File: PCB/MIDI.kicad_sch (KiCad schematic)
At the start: 17 parts, among them J6 MIDI Out, J7 MIDI In, U5 74LVC4245A, U6 6N137

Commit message: fixed PCB
 * Added 5.1k resistors to CC lines on USB-C port
 * Replaced diode OR thing and MOSFET with too low of a threshold voltage with a real OR gate and buffer
 * Fixed polarity of BNC output
 * Made headphone output not murderously loud and asymmetric
 * Added direct in/out to expansion pins
 * Reduced impedance into ADC for average volume level sensing
 * Increased MIDI input pullup resistance
 * Made thermal spokes to copper planes thinner
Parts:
- removed R22: 47, Resistor_SMD:R_0603_1608Metric_Pad0.98x0.95mm_HandSolder, symbol Device:R_US
- R21: value 47 -> 220
- renumbered D14 to D8
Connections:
- net MIDI In: now also R21.2
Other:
- moved on the sheet: R21
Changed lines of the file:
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@@
+    (stroke (width 0) (type default) (color 0 0 0 0))
+  )
+  (wire (pts (xy 99.695 76.2) (xy 99.695 80.01))
     (stroke (width 0) (type default) (color 0 0 0 0))
   )
@@
     (stroke (width 0) (type default) (color 0 0 0 0))
   )
+  (wire (pts (xy 99.695 80.01) (xy 118.745 80.01))
+    (stroke (width 0) (type default) (color 0 0 0 0))
+  )
+  (wire (pts (xy 99.695 64.77) (xy 99.695 68.58))
+    (stroke (width 0) (type default) (color 0 0 0 0))
+  )
   (wire (pts (xy 161.29 74.295) (xy 161.29 80.01))
     (stroke (width 0) (type default) (color 0 0 0 0))
@@
     (stroke (width 0) (type default) (color 0 0 0 0))
   )
+  (wire (pts (xy 118.745 64.77) (xy 118.745 74.93))
+    (stroke (width 0) (type default) (color 0 0 0 0))
+  )
+  (wire (pts (xy 149.86 113.665) (xy 145.415 113.665))
+    (stroke (width 0) (type default) (color 0 0 0 0))
+  )
+  (wire (pts (xy 149.86 114.935) (xy 149.86 113.665))
+    (stroke (width 0) (type default) (color 0 0 0 0))
+  )
+  (wire (pts (xy 167.64 121.92) (xy 167.64 123.825))
+    (stroke (width 0) (type default) (color 0 0 0 0))
+  )
+  (wire (pts (xy 108.585 129.54) (xy 110.49 129.54))
+    (stroke (width 0) (type default) (color 0 0 0 0))
+  )
+  (wire (pts (xy 153.67 77.47) (xy 168.91 77.47))
+    (stroke (width 0) (type default) (color 0 0 0 0))
+  )
+  (wire (pts (xy 125.095 118.11) (xy 125.095 123.825))
+    (stroke (width 0) (type default) (color 0 0 0 0))
+  )
+  (wire (pts (xy 108.585 118.11) (xy 108.585 123.825))
+    (stroke (width 0) (type default) (color 0 0 0 0))
+  )
+  (wire (pts (xy 133.985 85.09) (xy 138.43 85.09))
+    (stroke (width 0) (type default) (color 0 0 0 0))
+  )
   (wire (pts (xy 96.52 80.01) (xy 99.695 80.01))
-    (stroke (width 0) (type default) (color 0 0 0 0))
-  )
-  (wire (pts (xy 118.745 64.77) (xy 118.745 74.93))
-    (stroke (width 0) (type default) (color 0 0 0 0))
-  )
-  (wire (pts (xy 149.86 113.665) (xy 145.415 113.665))
-    (stroke (width 0) (type default) (color 0 0 0 0))
-  )
-  (wire (pts (xy 149.86 114.935) (xy 149.86 113.665))
-    (stroke (width 0) (type default) (color 0 0 0 0))
-  )
-  (wire (pts (xy 167.64 121.92) (xy 167.64 123.825))
-    (stroke (width 0) (type default) (color 0 0 0 0))
-  )
-  (wire (pts (xy 108.585 129.54) (xy 110.49 129.54))
-    (stroke (width 0) (type default) (color 0 0 0 0))
-  )
-  (wire (pts (xy 153.67 77.47) (xy 168.91 77.47))
-    (stroke (width 0) (type default) (color 0 0 0 0))
-  )
-  (wire (pts (xy 125.095 118.11) (xy 125.095 123.825))
-    (stroke (width 0) (type default) (color 0 0 0 0))
-  )
-  (wire (pts (xy 108.585 118.11) (xy 108.585 123.825))
-    (stroke (width 0) (type default) (color 0 0 0 0))
-  )
-  (wire (pts (xy 133.985 85.09) (xy 138.43 85.09))
-    (stroke (width 0) (type default) (color 0 0 0 0))
-  )
-  (wire (pts (xy 99.695 80.01) (xy 118.745 80.01))
     (stroke (width 0) (type default) (color 0 0 0 0))
   )
@@
   (symbol (lib_id "Device:D") (at 138.43 81.28 270) (unit 1)
     (in_bom yes) (on_board yes) (fields_autoplaced)
-    (property "Reference" "D14" (id 0) (at 140.462 81.7138 90)
+    (property "Reference" "D8" (id 0) (at 140.462 81.7138 90)
       (effects (font (size 1.27 1.27)) (justify left))
     )
@@
     (pin "2")
   )
-  (symbol (lib_id "Device:R_US") (at 99.695 76.2 0) (unit 1)
-    (in_bom yes) (on_board yes) (fields_autoplaced)
-    (property "Reference" "R22" (id 0) (at 101.346 75.3653 0)
-      (effects (font (size 1.27 1.27)) (justify left))
-    )
-    (property "Value" "47" (id 1) (at 101.346 77.9022 0)
-      (effects (font (size 1.27 1.27)) (justify left))
-    )
-    (property "Footprint" "Resistor_SMD:R_0603_1608Metric_Pad0.98x0.95mm_HandSolder" (id 2) (at 100.711 76.454 90)
-      (effects (font (size 1.27 1.27)) hide)
-    )
-    (property "Datasheet" "~" (id 3) (at 99.695 76.2 0)
-      (effects (font (size 1.27 1.27)) hide)
-    )
-    (pin "1")
-    (pin "2")
-  )
   (symbol (lib_id "Device:FerriteBead_Small") (at 151.13 77.47 270) (unit 1)
     (in_bom yes) (on_board yes) (fields_autoplaced)
@@
     (pin "2")
   )
-  (symbol (lib_id "Device:R_US") (at 99.695 68.58 0) (unit 1)
-    (in_bom yes) (on_board yes) (fields_autoplaced)
-    (property "Reference" "R21" (id 0) (at 101.346 67.7453 0)
+  (symbol (lib_id "Device:R_US") (at 99.695 72.39 0) (unit 1)
+    (in_bom yes) (on_board yes) (fields_autoplaced)
+    (property "Reference" "R21" (id 0) (at 101.346 71.5553 0)
       (effects (font (size 1.27 1.27)) (justify left))
     )
-    (property "Value" "47" (id 1) (at 101.346 70.2822 0)
+    (property "Value" "220" (id 1) (at 101.346 74.0922 0)
       (effects (font (size 1.27 1.27)) (justify left))
     )
-    (property "Footprint" "Resistor_SMD:R_0603_1608Metric_Pad0.98x0.95mm_HandSolder" (id 2) (at 100.711 68.834 90)
-      (effects (font (size 1.27 1.27)) hide)
-    )
-    (property "Datasheet" "~" (id 3) (at 99.695 68.58 0)
-      (effects (font (size 1.27 1.27)) hide)
-    )
+    (property "Footprint" "Resistor_SMD:R_0603_1608Metric_Pad0.98x0.95mm_HandSolder" (id 2) (at 100.711 72.644 90)
+      (effects (font (size 1.27 1.27)) hide)
+    )
+    (property "Datasheet" "~" (id 3) (at 99.695 72.39 0)
+      (effects (font (size 1.27 1.27)) hide)
+    )

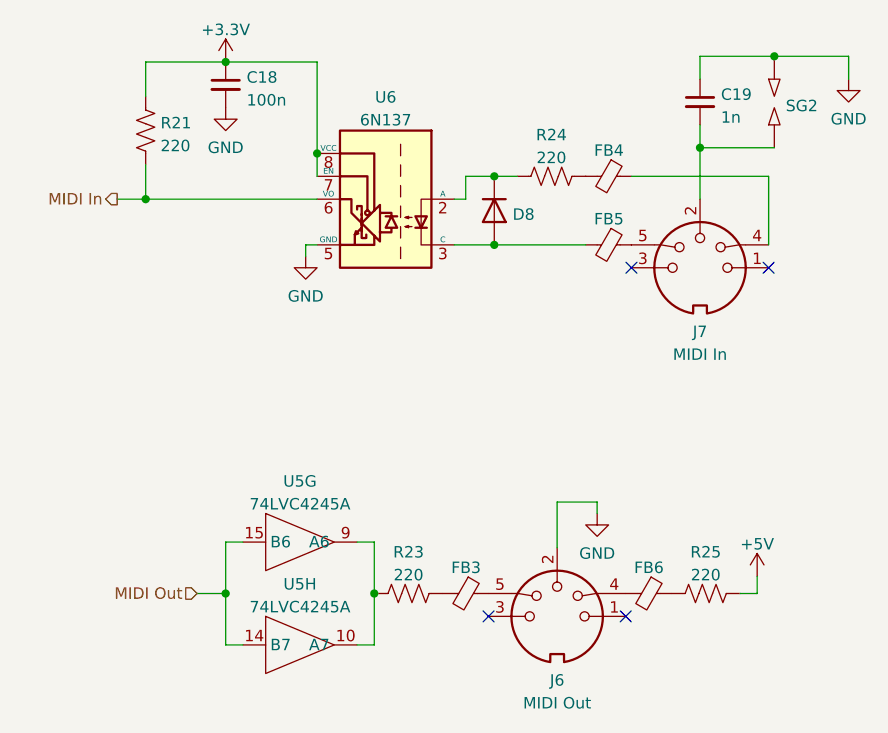
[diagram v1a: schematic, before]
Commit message: improved power line filtering
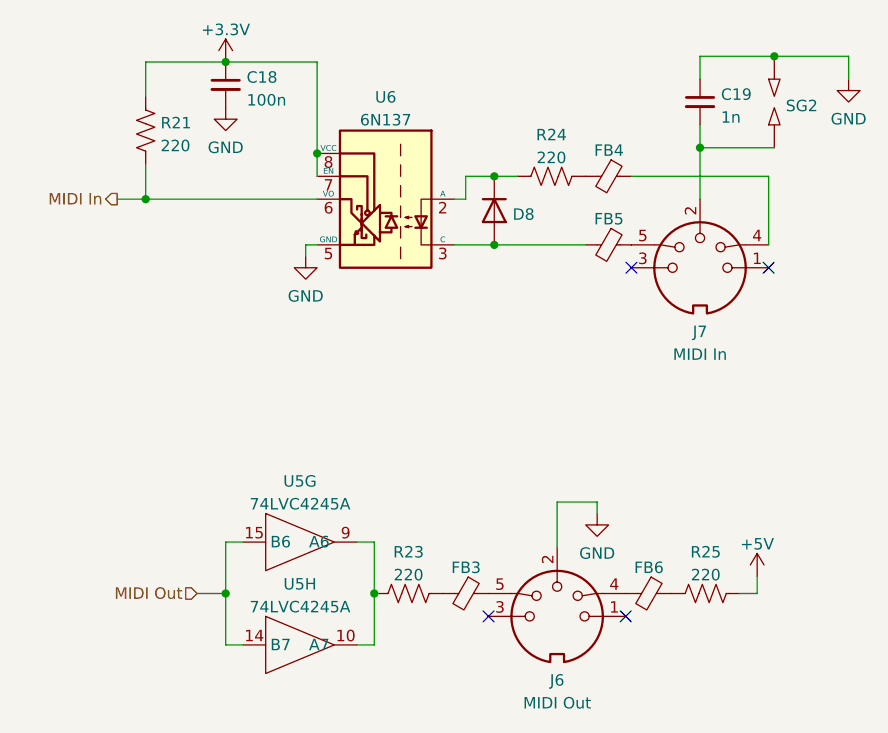
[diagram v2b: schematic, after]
